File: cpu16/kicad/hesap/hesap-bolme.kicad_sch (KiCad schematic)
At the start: 80 parts, among them U44 74HC283, U45 74HC283, U46 74HC157, U47 74HC157, U48 74HC283, U49 74HC283, U50 74HC157, U51 74HC157, U52 74HC283, U53 74HC283, U54 74HC157, U55 74HC157, U56 74HC283, U57 74HC283, U58 74HC157, U59 74HC157, U60 74HC283, U61 74HC283, U62 74HC157, U63 74HC157, U64 74HC283, U65 74HC283, U66 74HC157, U67 74HC157, U68 74HC283, U69 74HC283, U70 74HC157, U71 74HC157, U72 74HC283, U73 74HC283, U74 74HC157, U75 74HC157, U76 74HC08, U77 74HC32, U78 74HC32, U79 74HC00, U80 74HC04, U81 74HC04, U82 74HC30

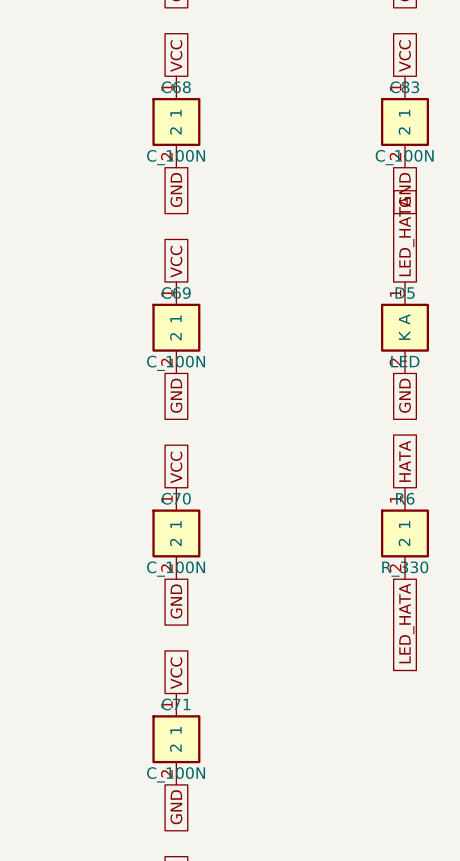
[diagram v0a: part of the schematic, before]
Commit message: Hesap makinesi: eksi işareti sonucun solunda, lamba testinde de yanar; HATA LED'i göstergelerin yanında
- işaret hanesi (DS7) sonucun hanelerinden önce yerleşir: 3D kartta ve
  şemada en solda
- ISARET_g = NEG + lamba testi (boş kapı birimleriyle, çip sayısı aynı)
- HATA LED'i Bölme bloğundan "Gösterge: Sonuç" bloğuna
- rehber ve tasarım belgesi güncellendi

Co-Authored-By: Claude Opus 5.5 (1M context) <noreply@anthropic.com>
Claude-Session: https://claude.ai/code/session_018J8WVuECVRbQJyCbmF6Nsi
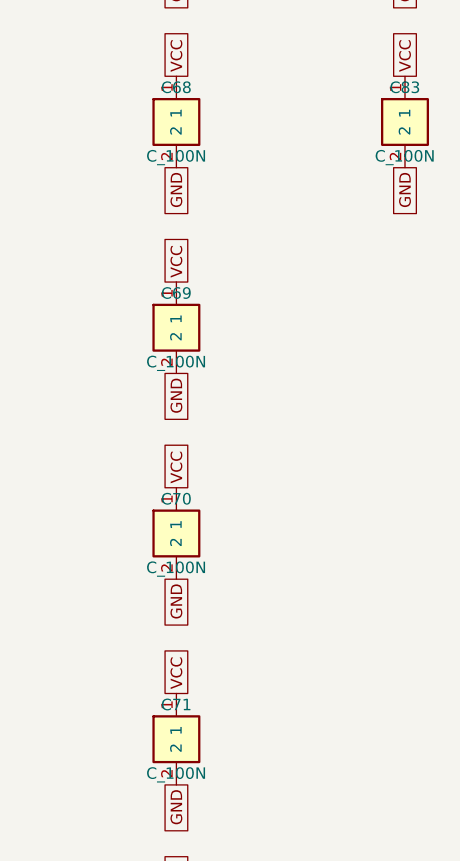
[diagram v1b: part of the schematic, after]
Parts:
- removed D5: LED, LED_THT:LED_D3.0mm, symbol cpu16:LED
- removed R6: R_330, Resistor_THT:R_Axial_DIN0207_L6.3mm_D2.5mm_P7.62mm_Horizontal, symbol cpu16:R_330
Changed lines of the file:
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@@
     (instances (project "hesap" (path "/2eee201d-0000-4000-8000-000000000001/b6103959-0000-4000-8000-000000000005" (reference "C83") (unit 1))))
-  )
-  (symbol (lib_id "cpu16:LED") (at 528.32 99.06 0) (unit 1)
-    (in_bom yes) (on_board yes) (dnp no)
-    (property "Reference" "D5" (at 528.32 95.25 0) (effects (font (size 1.27 1.27))))
-    (property "Value" "LED" (at 528.32 102.87 0) (effects (font (size 1.27 1.27))))
-    (property "Footprint" "LED_THT:LED_D3.0mm" (at 528.32 99.06 0) (effects (font (size 1.27 1.27)) hide))
-    (property "Datasheet" "" (at 528.32 99.06 0) (effects (font (size 1.27 1.27)) hide))
-    (property "Gorev" "HATA LED'i" (at 528.32 99.06 0) (effects (font (size 1.27 1.27)) hide))
-    (pin "1")
-    (pin "2")
-    (instances (project "hesap" (path "/2eee201d-0000-4000-8000-000000000001/b6103959-0000-4000-8000-000000000005" (reference "D5") (unit 1))))
-  )
-  (symbol (lib_id "cpu16:R_330") (at 528.32 121.92 0) (unit 1)
-    (in_bom yes) (on_board yes) (dnp no)
-    (property "Reference" "R6" (at 528.32 118.11 0) (effects (font (size 1.27 1.27))))
-    (property "Value" "R_330" (at 528.32 125.73 0) (effects (font (size 1.27 1.27))))
-    (property "Footprint" "Resistor_THT:R_Axial_DIN0207_L6.3mm_D2.5mm_P7.62mm_Horizontal" (at 528.32 121.92 0) (effects (font (size 1.27 1.27)) hide))
-    (property "Datasheet" "" (at 528.32 121.92 0) (effects (font (size 1.27 1.27)) hide))
-    (property "Gorev" "HATA LED direnci" (at 528.32 121.92 0) (effects (font (size 1.27 1.27)) hide))
-    (pin "1")
-    (pin "2")
-    (instances (project "hesap" (path "/2eee201d-0000-4000-8000-000000000001/b6103959-0000-4000-8000-000000000005" (reference "R6") (unit 1))))
   )
   (global_label "NB1" (shape passive) (at 45.72 53.34 180) (fields_autoplaced) (effects (font (size 1.27 1.27)) (justify right))
@@
   (global_label "GND" (shape passive) (at 528.32 81.28 270) (fields_autoplaced) (effects (font (size 1.27 1.27)) (justify right))
     (property "Intersheetrefs" "${INTERSHEET_REFS}" (at 528.32 81.28 0) (effects (font (size 1.27 1.27)) hide)))
-  (global_label "LED_HATA" (shape passive) (at 528.32 93.98 90) (fields_autoplaced) (effects (font (size 1.27 1.27)) (justify left))
-    (property "Intersheetrefs" "${INTERSHEET_REFS}" (at 528.32 93.98 0) (effects (font (size 1.27 1.27)) hide)))
-  (global_label "GND" (shape passive) (at 528.32 104.14 270) (fields_autoplaced) (effects (font (size 1.27 1.27)) (justify right))
-    (property "Intersheetrefs" "${INTERSHEET_REFS}" (at 528.32 104.14 0) (effects (font (size 1.27 1.27)) hide)))
-  (global_label "HATA" (shape passive) (at 528.32 116.84 90) (fields_autoplaced) (effects (font (size 1.27 1.27)) (justify left))
-    (property "Intersheetrefs" "${INTERSHEET_REFS}" (at 528.32 116.84 0) (effects (font (size 1.27 1.27)) hide)))
-  (global_label "LED_HATA" (shape passive) (at 528.32 127 270) (fields_autoplaced) (effects (font (size 1.27 1.27)) (justify right))
-    (property "Intersheetrefs" "${INTERSHEET_REFS}" (at 528.32 127 0) (effects (font (size 1.27 1.27)) hide)))
 )
